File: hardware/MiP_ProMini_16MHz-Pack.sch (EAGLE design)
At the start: 51 parts, among them Q1 16MHZ, U1 ATMEGA328, U2 MIC5205-5.0, U3 TS3USB221A, U4 MIC5205-3.3

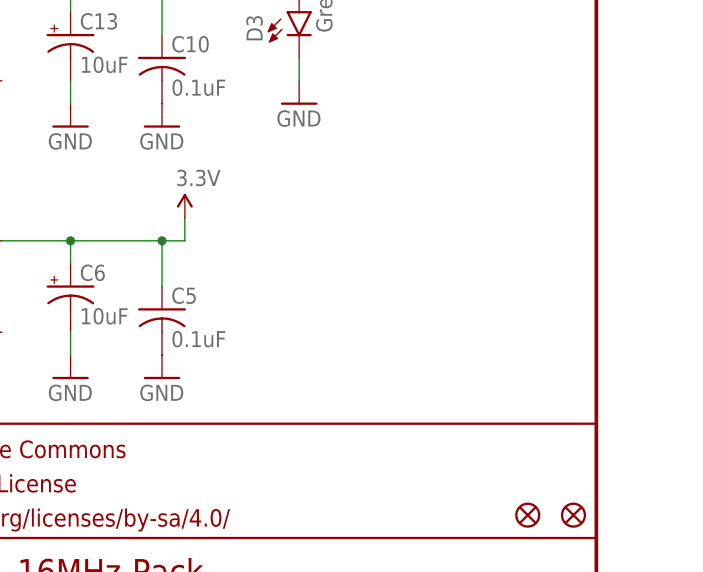
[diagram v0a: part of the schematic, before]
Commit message: Add a 1k load across 3.3V supply
Without this load, the 3.3V supply was closer to 4.4V. The datasheet
for the regulator indicates that it doesn't have a minimum load to
maintain regulation but it also indicates that the output capacitance
can be closer to 0.5uF when the output current is only 1mA. If a
person was using the 3.3V supply for something else that was putting
a >= 1mA load on it then they could omit this resistor. Lowering the
output capacitance (which was copied from the original Sparkfun design)
might also correct the problem.
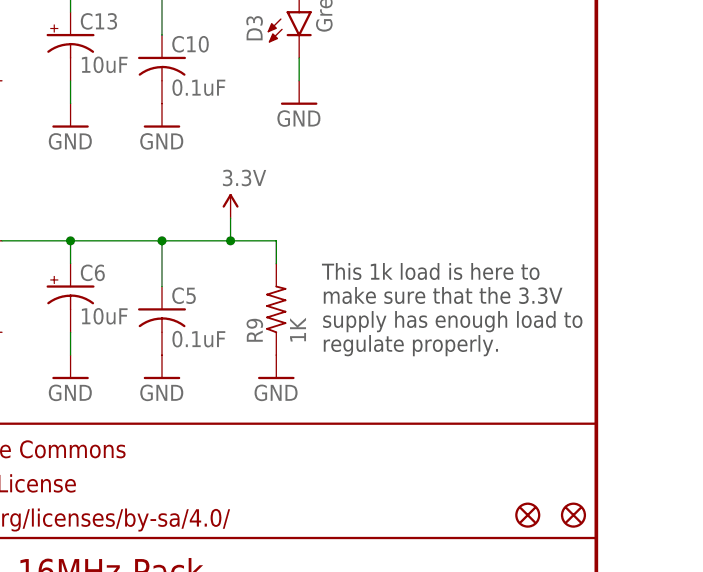
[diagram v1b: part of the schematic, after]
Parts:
- added R9: 1K, rcl:R-US_R0805
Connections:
- net 3.3V: now also R9.2
- net GND: now also R9.1
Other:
- note added: "This 1k load is here to make sure that the 3.3V supply has enough load to regulate properly."
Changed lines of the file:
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@@
 <part name="P+5" library="SparkFun-Aesthetics" deviceset="3.3V" device="" value="3.3V"/>
 <part name="P+16" library="SparkFun-Aesthetics" deviceset="5V" device="" value="5V"/>
+<part name="R9" library="rcl" deviceset="R-US_" device="R0805" value="1K"/>
+<part name="GND18" library="SparkFun" deviceset="GND" device=""/>
 </parts>
 <sheets>
@@
 <text x="36.322" y="169.418" size="1.27" layer="97">Short J1 to power
 board from FTDI.</text>
+<text x="218.44" y="53.34" size="1.778" layer="97" align="top-left">This 1k load is here to
+make sure that the 3.3V
+supply has enough load to
+regulate properly.</text>
 </plain>
 <instances>
@@
 <instance part="GND16" gate="1" x="160.02" y="40.64"/>
 <instance part="GND17" gate="1" x="152.4" y="40.64"/>
-<instance part="P+9" gate="G$1" x="203.2" y="58.42"/>
+<instance part="P+9" gate="G$1" x="208.28" y="58.42"/>
 <instance part="J1" gate="G$1" x="45.72" y="160.02" rot="R90"/>
 <instance part="P+10" gate="G$1" x="50.8" y="172.72"/>
@@
 </instance>
 <instance part="P+16" gate="G$1" x="111.76" y="68.58"/>
+<instance part="R9" gate="G$1" x="213.36" y="48.26" rot="R90"/>
+<instance part="GND18" gate="1" x="213.36" y="40.64"/>
 </instances>
 <busses>
@@
 <pinref part="GND17" gate="1" pin="GND"/>
 </segment>
+<segment>
+<pinref part="R9" gate="G$1" pin="1"/>
+<pinref part="GND18" gate="1" pin="GND"/>
+</segment>
 </net>
 <net name="AREF" class="0">
@@
 <net name="3.3V" class="0">
 <segment>
+<pinref part="C4" gate="G$1" pin="2"/>
+<pinref part="P+7" gate="G$1" pin="3.3V"/>
+</segment>
+<segment>
+<pinref part="U3" gate="G$1" pin="VCC"/>
+<pinref part="P+6" gate="G$1" pin="3.3V"/>
+<wire x1="35.56" y1="149.86" x2="33.02" y2="149.86" width="0.1524" layer="91"/>
+<wire x1="33.02" y1="149.86" x2="33.02" y2="152.4" width="0.1524" layer="91"/>
+</segment>
+<segment>
+<pinref part="D1" gate="G$1" pin="C"/>
+<pinref part="P+12" gate="G$1" pin="3.3V"/>
+<wire x1="60.96" y1="170.18" x2="60.96" y2="172.72" width="0.1524" layer="91"/>
+</segment>
+<segment>
+<pinref part="SJ1" gate="G$1" pin="3"/>
+<pinref part="P+14" gate="G$1" pin="3.3V"/>
+<wire x1="33.02" y1="68.58" x2="33.02" y2="66.04" width="0.1524" layer="91"/>
+<junction x="33.02" y="66.04"/>
+</segment>
+<segment>
+<pinref part="SJ2" gate="G$1" pin="3"/>
+<pinref part="P+5" gate="G$1" pin="3.3V"/>
+<wire x1="106.68" y1="68.58" x2="106.68" y2="66.04" width="0.1524" layer="91"/>
+</segment>
+<segment>
 <pinref part="U4" gate="G$1" pin="OUT"/>
-<pinref part="P+9" gate="G$1" pin="3.3V"/>
 <wire x1="182.88" y1="55.88" x2="190.5" y2="55.88" width="0.1524" layer="91"/>
 <wire x1="190.5" y1="55.88" x2="200.66" y2="55.88" width="0.1524" layer="91"/>
-<wire x1="200.66" y1="55.88" x2="203.2" y2="55.88" width="0.1524" layer="91"/>
-<wire x1="203.2" y1="55.88" x2="203.2" y2="58.42" width="0.1524" layer="91"/>
 <pinref part="C6" gate="G$1" pin="+"/>
 <wire x1="190.5" y1="53.34" x2="190.5" y2="55.88" width="0.1524" layer="91"/>
@@
 <pinref part="C5" gate="G$1" pin="1"/>
 <wire x1="200.66" y1="50.8" x2="200.66" y2="55.88" width="0.1524" layer="91"/>
+<pinref part="R9" gate="G$1" pin="2"/>
+<wire x1="200.66" y1="55.88" x2="208.28" y2="55.88" width="0.1524" layer="91"/>
+<wire x1="208.28" y1="55.88" x2="213.36" y2="55.88" width="0.1524" layer="91"/>
+<wire x1="213.36" y1="55.88" x2="213.36" y2="53.34" width="0.1524" layer="91"/>
 <junction x="200.66" y="55.88"/>
-</segment>
-<segment>
-<pinref part="C4" gate="G$1" pin="2"/>
-<pinref part="P+7" gate="G$1" pin="3.3V"/>
-</segment>
-<segment>
-<pinref part="U3" gate="G$1" pin="VCC"/>
-<pinref part="P+6" gate="G$1" pin="3.3V"/>
-<wire x1="35.56" y1="149.86" x2="33.02" y2="149.86" width="0.1524" layer="91"/>
-<wire x1="33.02" y1="149.86" x2="33.02" y2="152.4" width="0.1524" layer="91"/>
-</segment>
-<segment>
-<pinref part="D1" gate="G$1" pin="C"/>
-<pinref part="P+12" gate="G$1" pin="3.3V"/>
-<wire x1="60.96" y1="170.18" x2="60.96" y2="172.72" width="0.1524" layer="91"/>
-</segment>
-<segment>
-<pinref part="SJ1" gate="G$1" pin="3"/>
-<pinref part="P+14" gate="G$1" pin="3.3V"/>
-<wire x1="33.02" y1="68.58" x2="33.02" y2="66.04" width="0.1524" layer="91"/>
-<junction x="33.02" y="66.04"/>
-</segment>
-<segment>
-<pinref part="SJ2" gate="G$1" pin="3"/>
-<pinref part="P+5" gate="G$1" pin="3.3V"/>
-<wire x1="106.68" y1="68.58" x2="106.68" y2="66.04" width="0.1524" layer="91"/>
-</segment>
-</net>
+<pinref part="P+9" gate="G$1" pin="3.3V"/>
+<wire x1="208.28" y1="58.42" x2="208.28" y2="55.88" width="0.1524" layer="91"/>
+<junction x="208.28" y="55.88"/>
+</segment>
+</net>

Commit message: Update PCB design to version 4
This version update includes:
* The original Murata resonator is no longer available and the
  suggested replacement on Digikey has slightly different pad spacing.
  This commit includes BOM, documentation, and part footprint updates
  for the resonator.
* I tinted the via under R10 as I had recently shorted the bottom of
  R10 to this via by putting too much solder on the pad.

NOTE: I haven't yet had these boards made by OSHPark and tested them
      but I wanted to make these updates while they were still fresh
      in my mind.
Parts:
- Q1: device adam_custom:RESONATORMURATA_16MHZ -> adam_custom:RESONATORMURATA_16MHZ_2
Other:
- note added: "v4"
- note removed: "v3"
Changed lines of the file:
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@@
 <part name="S1" library="adam_custom" deviceset="SWITCH-MOMENTARY-NO" device="SMD" value="Reset"/>
 <part name="JP3" library="SparkFun" deviceset="M02" device="PTH"/>
-<part name="Q1" library="adam_custom" deviceset="RESONATOR" device="MURATA_16MHZ" value="16MHZ"/>
+<part name="Q1" library="adam_custom" deviceset="RESONATOR" device="MURATA_16MHZ_2" value="16MHZ"/>
 <part name="FRAME1" library="SparkFun-Aesthetics" deviceset="FRAME-LETTER" device=""/>
 <part name="GND1" library="SparkFun" deviceset="GND" device=""/>
@@
 <text x="243.84" y="141.478" size="1.778" layer="97" rot="R90">Optional Pullups for I2C lines</text>
 <text x="166.37" y="11.43" size="2.54" layer="94">Adam Green (http://github.com/adamgreen)</text>
-<text x="238.76" y="7.62" size="2.54" layer="94">v3</text>
+<text x="238.76" y="7.62" size="2.54" layer="94">v4</text>
 <text x="86.36" y="154.94" size="1.778" layer="97">Note: Cut jumper to move
 SEL to another pin</text>
